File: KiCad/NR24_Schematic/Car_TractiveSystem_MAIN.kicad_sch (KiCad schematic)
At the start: 19 parts, among them J1 M_con, J2 F_con, K2 Key Switch Relay, M1 Zero_7R_Motor, SW1 12V E-stop, SW3 GLVMS, SW4 Break Over Travel, SW7 TSMS, SW8 12V E-stop, U1 Sevcon_Gen4_Size6, U2 Throttle, U4 Vehicle Dynamic Module, U6 AEMnet_Logger, U7 Brake Pressure Sensor (Aim)

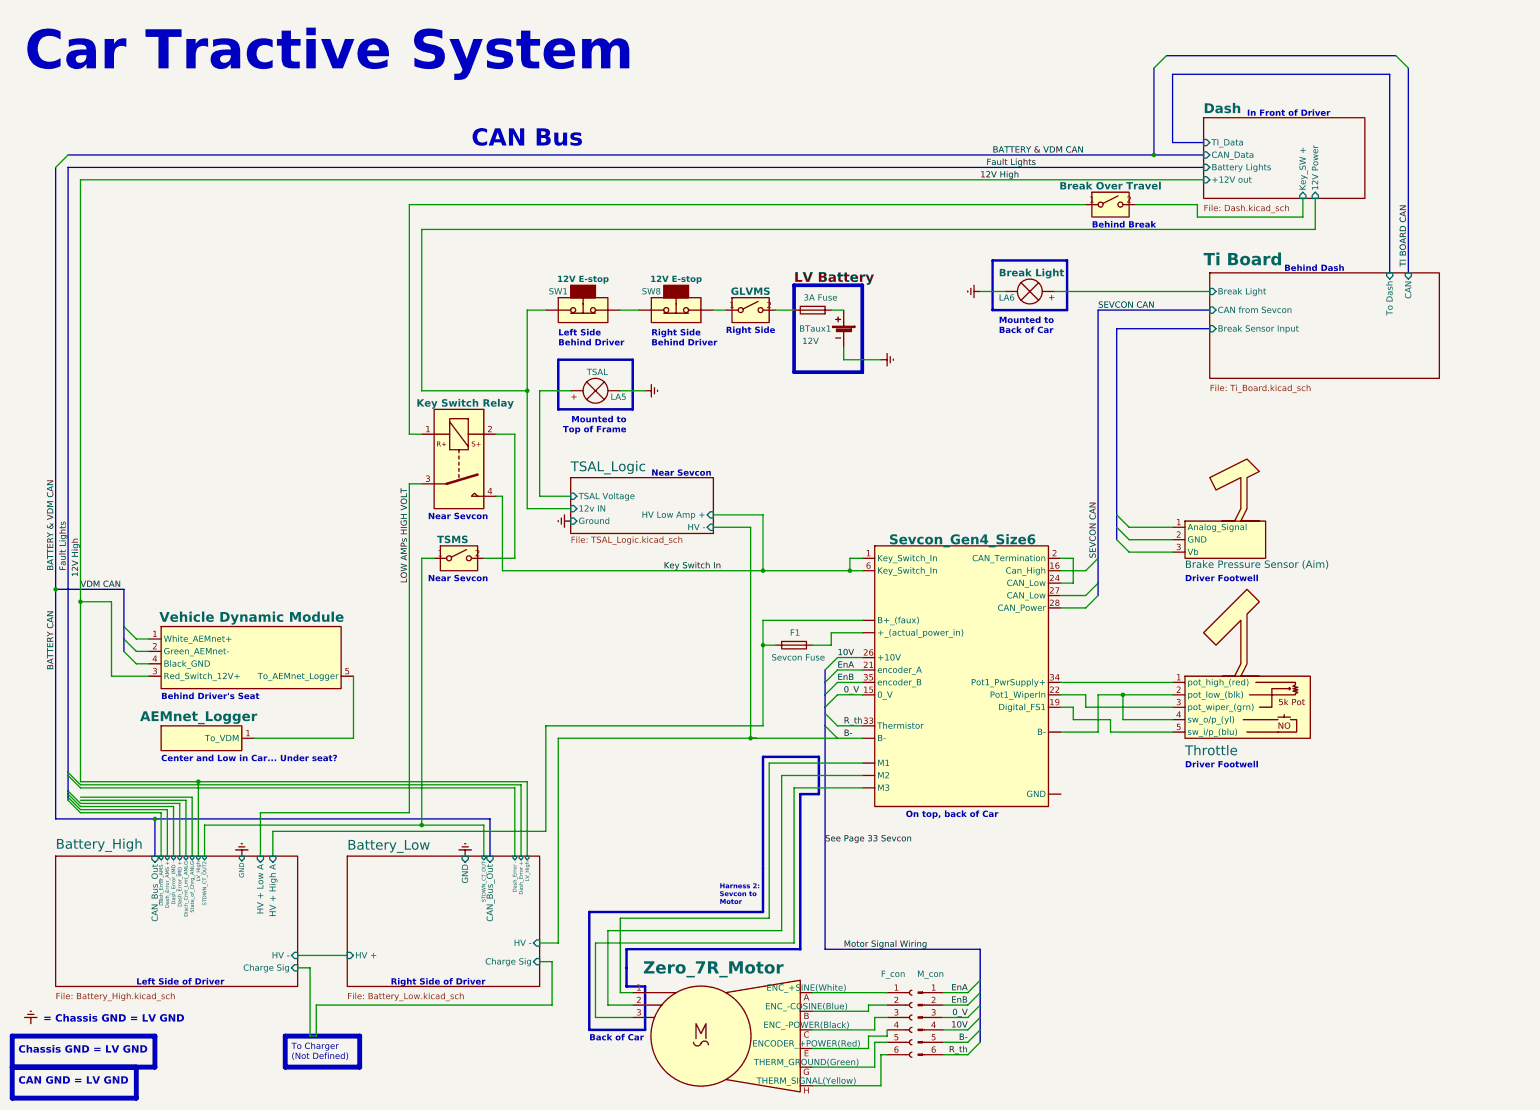
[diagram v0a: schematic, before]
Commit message: added accumulator info
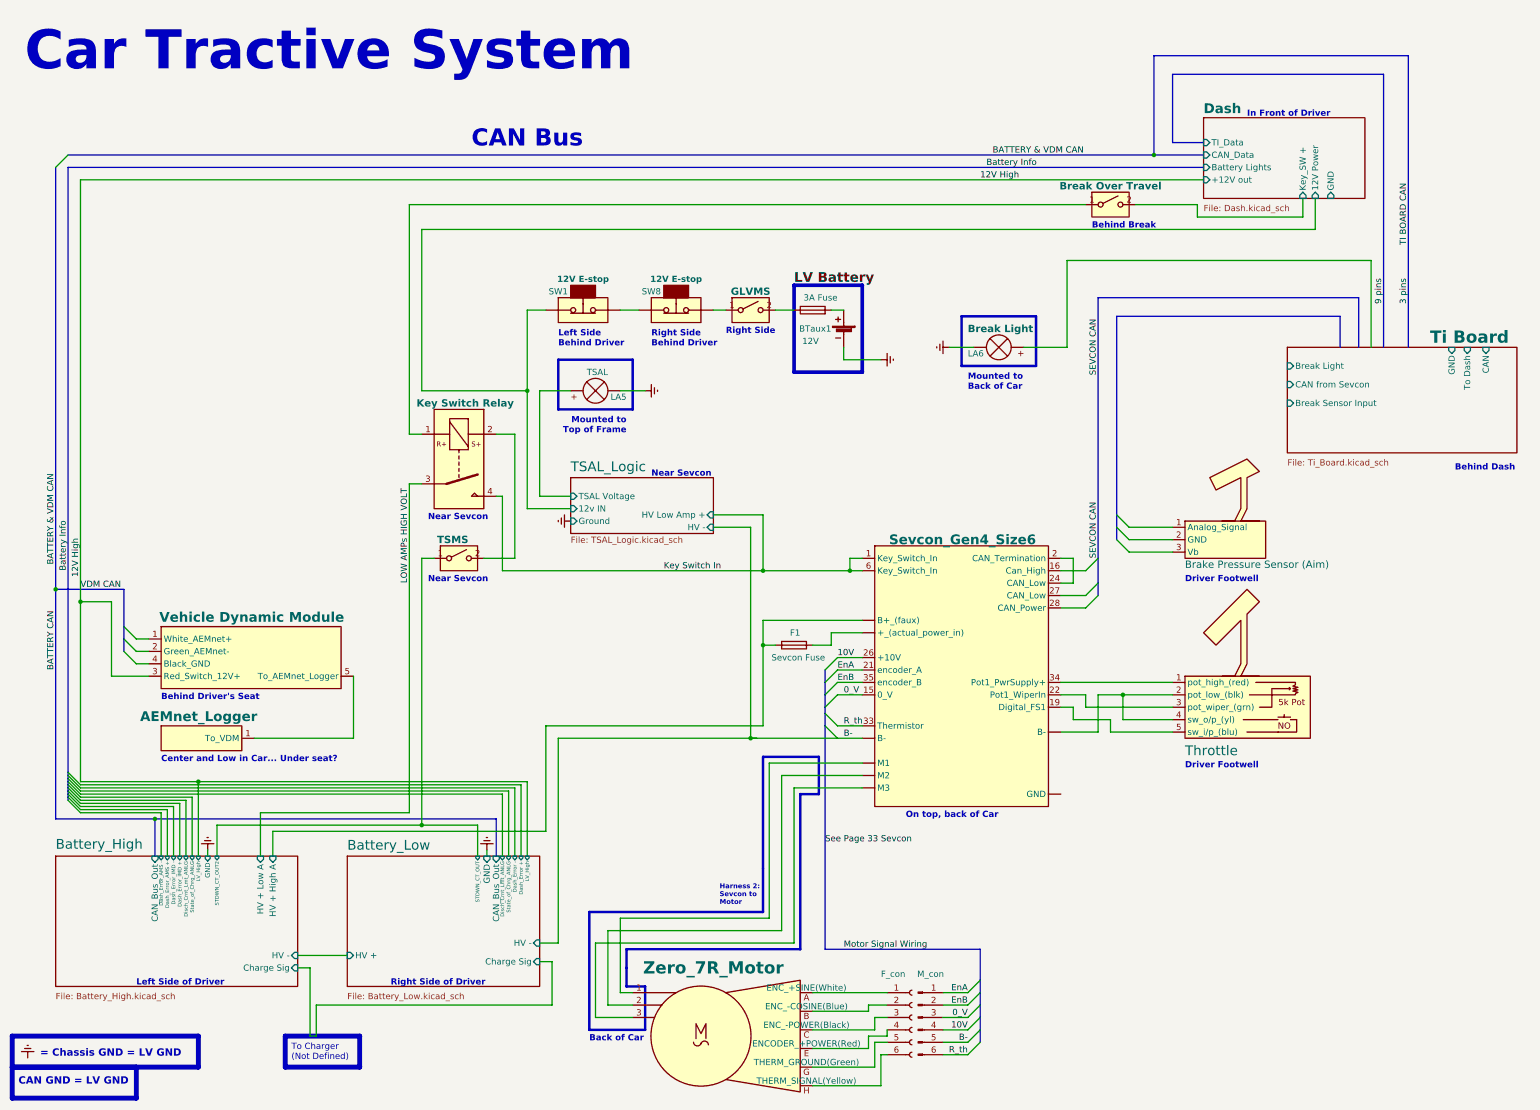
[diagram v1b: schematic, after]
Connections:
- net Ti Board/Break Light: no longer LA6.2 (+)
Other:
- sheet Battery_Low ports: added Disch_Crnt_Lmt_ANLG, State_of_Chrg_ANLG; removed none
- sheet Dash ports: added GND; removed none
- sheet Ti Board ports: added GND; removed none
- note removed: "Chassis GND = LV GND"
- moved on the sheet: LA6

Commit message: first iteration
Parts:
- added J3, J4: Female Box Side, symbol Connector:DA15_Receptacle
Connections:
- net  VDM CAN: now also J3.8, J4.8
- net Earth: now also J3.1, J4.1
- net Battery_High/STDWN_CT_OUT2 renamed Battery_High/STDWN_CT_OUT2         
- net Battery_High/STDWN_CT_OUT2         : now also J3.7, J4.7
- new net Battery_High/Dash_Error_AMS +         : J3.3
- new net Battery_High/Dash_Error_AMS -         : J3.10 (P10)
- new net Battery_High/Dash_Error_IMD +         : J3.2
- new net Battery_High/Dash_Error_IMD -         : J3.9 (P9)
- new net Battery_Low/Dash_Error +         : J4.9 (P9)
- new net Battery_Low/Dash_Error -         : J4.2
- new net CAN H / L / G: J3.12 (P12), J4.12 (P12)
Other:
- sheet Battery_High ports: added CAN_Bus_Out     , Dash_Error_AMS +         , Dash_Error_AMS -         , Dash_Error_IMD +         , Dash_Error_IMD -         , GND      , LV_High         , STDWN_CT_OUT2         ; removed CAN_Bus_Out, Dash_Error_AMS +, Dash_Error_AMS -, Dash_Error_IMD +, Dash_Error_IMD -, Disch_Crnt_Lmt_ANLG, GND, LV_High, STDWN_CT_OUT2, State_of_Chrg_ANLG
- sheet Battery_Low ports: added CAN_Bus_Out     , Dash_Error +         , Dash_Error -         , GND      , LV_High         , STDWN_CT_OUT         ; removed CAN_Bus_Out, Dash_Error +, Dash_Error -, Disch_Crnt_Lmt_ANLG, GND, LV_High, STDWN_CT_OUT, State_of_Chrg_ANLG

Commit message: Update Car_TractiveSystem_MAIN.kicad_sch
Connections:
- net Battery_High/CAN_Bus_Out     : now also J3.4
- net Battery_Low/CAN_Bus_Out     : now also J4.4
